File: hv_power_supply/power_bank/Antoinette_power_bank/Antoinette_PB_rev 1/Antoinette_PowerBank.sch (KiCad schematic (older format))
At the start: 44 parts, among them J1 NanoFit_RA_TH_02, J2 USB-Micro-1981568-1, J3 NanoFit_RA_TH_02, J4 USB-A-S-X-X-SM2, J5 NanoFit_RA_TH_02, Q1 SSM3K333R, U2 MCP73871T-2CCI_ML, U3 TPS61090RSAR

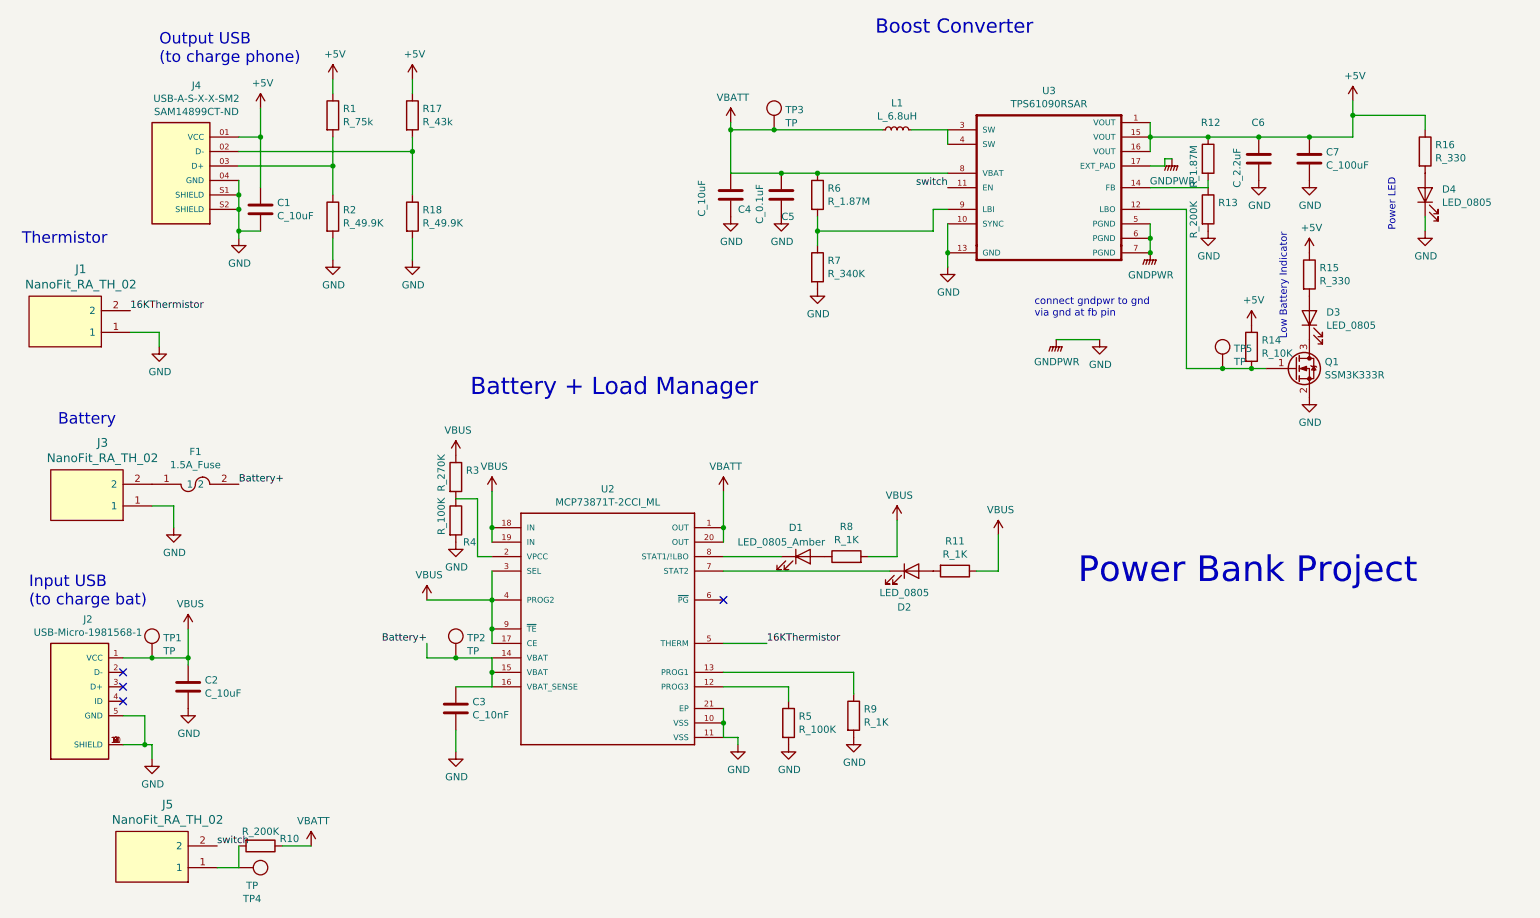
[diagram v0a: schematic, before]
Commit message: Add new files for updated pcb.
Added files for updated pcb with new inductor and series/parallel resistors for the 10k thermistor.
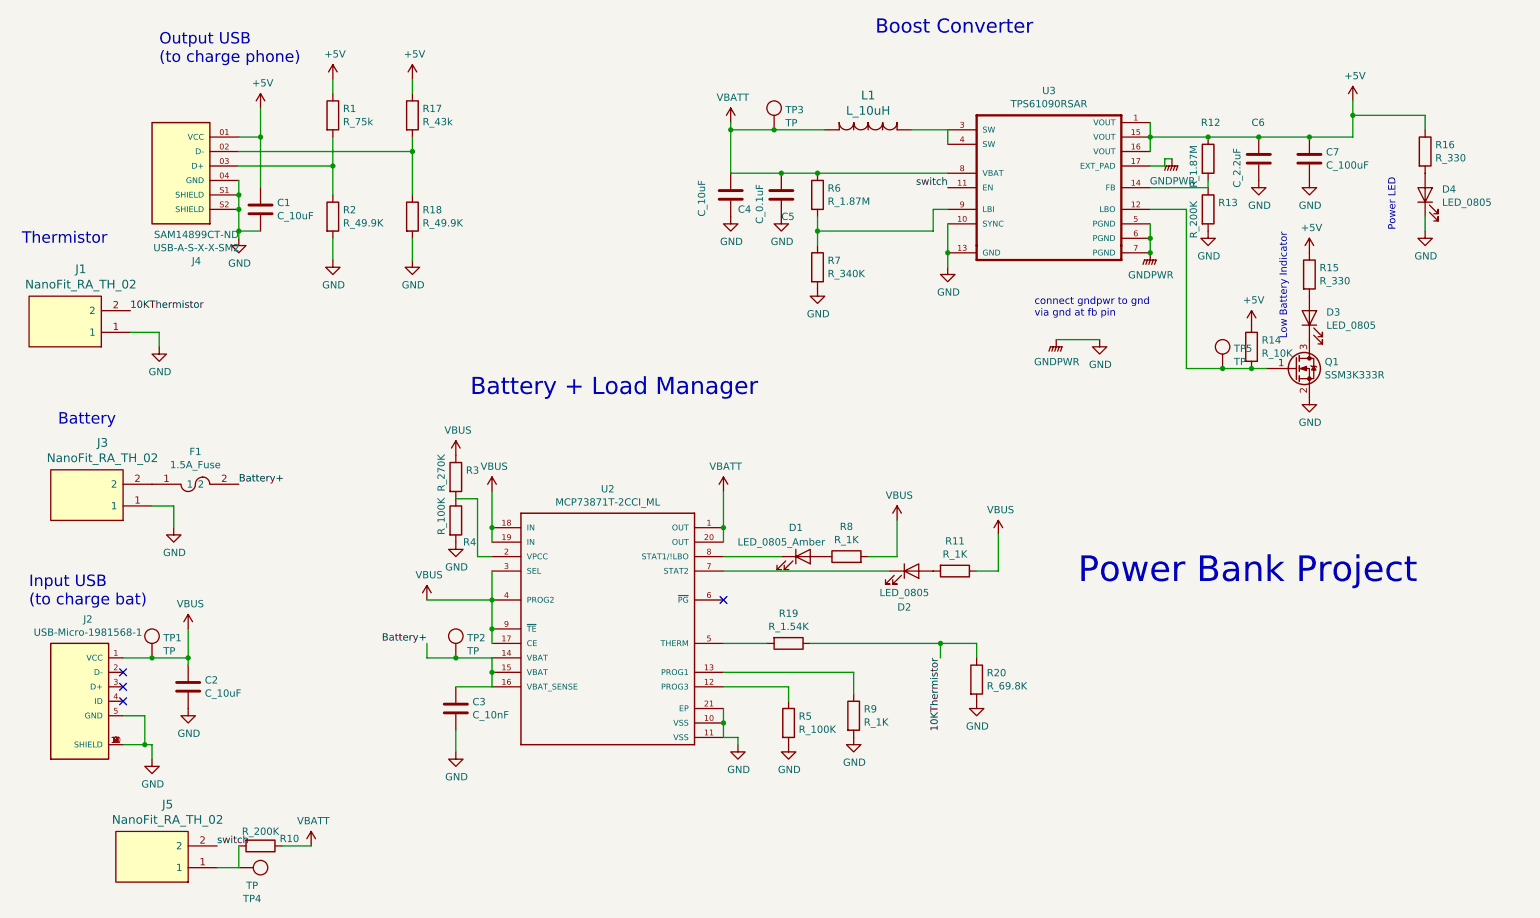
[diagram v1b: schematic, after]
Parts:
- removed L1: L_6.8uH, footprints:L_100uH_OEM, symbol formula:L_6.8uH
- added L1: L_10uH, footprints:BournsInductor, symbol formula:L_10uH
- added R19: R_1.54K, footprints:R_0805_OEM, symbol formula:R_1.54K
- added R20: R_69.8K, footprints:R_0805_OEM, symbol formula:R_69.8K
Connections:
- net +BATT: now also L1.2
- net GND: now also R20.2
- net at U3.3 (SW), U3.4 (SW): now also L1.1
- net 16KThermistor: no longer names the net of U2.5 (THERM)
- net 16KThermistor: now also R19.2; no longer J1.2
- new net 10KThermistor: J1.2, R19.1, R20.1
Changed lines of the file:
@@
 	1750 2900 1750 3000
 Text Label 1550 2750 0    50   ~ 0
-16KThermistor
+10KThermistor
 Text Label 2300 3950 0    50   ~ 0
 Battery+
@@
 	1    0    0    -1
 $EndComp
-$Comp
-L formula:L_6.8uH L1
-U 1 1 5F93B925
-P 6850 1500
-F 0 "L1" H 6850 1685 50  0000 C CNN
-F 1 "L_6.8uH" H 6850 1594 50  0000 C CNN
-F 2 "footprints:L_100uH_OEM" H 6750 1300 50  0001 C CNN
-F 3 "" H 6750 1350 50  0001 C CNN
-F 4 "Digikey" H 6950 1300 50  0001 C CNN "MFN"
-F 5 "445-1539-1-ND" H 6850 1750 50  0001 C CNN "MPN"
-	1    6850 1500
-	1    0    0    -1
-$EndComp
 Wire Wire Line
 	7200 1500 6950 1500
@@
 Wire Wire Line
 	5650 5050 5950 5050
-Text Label 5950 5050 0    50   ~ 0
-16KThermistor
+Text Label 7150 5150 3    50   ~ 0
+10KThermistor
 NoConn ~ 5650 4750
 Wire Wire Line
@@
 Text Notes 8100 4650 0    177  ~ 0
 Power Bank Project
-$Comp
-L formula:USB-A-S-X-X-SM2 J4
-U 1 1 5FB17265
-P 1900 1750
-F 0 "J4" H 1793 2307 50  0000 C CNN
-F 1 "USB-A-S-X-X-SM2" H 1793 2216 50  0000 C CNN
-F 2 "footprints:SAMTEC_USB-A-S-X-X-SM2" H 1900 1750 50  0001 L BNN
-F 3 "http://suddendocs.samtec.com/catalog_english/usb_a.pdf" H 1900 1750 50  0001 L BNN
-F 4 "Samtec" H 1900 1750 50  0001 L BNN "Field4"
-F 5 "Manufacturer Recommendations" H 1900 1750 50  0001 L BNN "Field5"
-F 6 "7.8 mm" H 1900 1750 50  0001 L BNN "Field6"
-F 7 "SAM14899CT-ND" H 1793 2125 50  0000 C CNN "MPN"
-	1    1900 1750
-	-1   0    0    -1
-$EndComp
 Wire Wire Line
 	1500 5750 1650 5750
-$Comp
-L formula:USB-Micro-1981568-1 J2
-U 1 1 5FB0DC42
-P 1200 5450
-F 0 "J2" H 1257 6017 50  0000 C CNN
-F 1 "USB-Micro-1981568-1" H 1257 5926 50  0000 C CNN
-F 2 "footprints:TE_1981568-1" H 1000 6000 50  0001 L BNN
-F 3 "https://www.te.com/commerce/DocumentDelivery/DDEController?Action=srchrtrv&DocNm=1981568&DocType=Customer+Drawing&DocLang=English" H 1200 5450 50  0001 L BNN
-F 4 ".65 mm[.025 in]" H 1150 6000 50  0001 L BNN "Field4"
-F 5 "Connector" H 600 5800 50  0001 L BNN "Field5"
-F 6 "1981568-1" H 1100 6000 50  0001 L BNN "Field6"
-F 7 "1981568-1" H 1350 5900 50  0001 C CNN "MPN"
-F 8 "https://www.digikey.com/en/products/detail/te-connectivity-amp-connectors/1981568-1/1786248?s=N4IgTCBcDaIIwE4AccCsA2JBaOIC6AvkA" H 1000 6000 50  0001 C CNN "Purchasing Link"
-	1    1200 5450
-	1    0    0    -1
-$EndComp
 Wire Wire Line
 	1500 5550 1650 5550
@@
 	5650 4000 5650 4250
 Wire Wire Line
-	2300 1850 2300 1950
-Wire Wire Line
 	5700 1800 6050 1800
 Wire Wire Line
@@
 Wire Wire Line
 	6300 1800 7200 1800
-Connection ~ 6000 1500
-Wire Wire Line
-	6000 1500 6750 1500
 Connection ~ 9700 1550
 Wire Wire Line
@@
 Wire Wire Line
 	7200 2350 7200 2450
-Connection ~ 2300 2050
-Wire Wire Line
-	2300 2050 2300 2200
-Connection ~ 2300 1950
-Wire Wire Line
-	2300 1950 2300 2050
 Connection ~ 5650 5600
 Wire Wire Line
@@
 	-1   0    0    1
 $EndComp
+$Comp
+L formula:USB-A-S-X-X-SM2 J4
+U 1 1 606F9F4E
+P 1900 1750
+F 0 "J4" H 1793 1093 50  0000 C CNN
+F 1 "USB-A-S-X-X-SM2" H 1793 1184 50  0000 C CNN
+F 2 "footprints:SAMTEC_USB-A-S-X-X-SM2" H 1900 1750 50  0001 L BNN
+F 3 "" H 1900 1750 50  0001 L BNN
+F 4 "Samtec" H 1900 1750 50  0001 L BNN "Field4"
+F 5 "Manufacturer Recommendations" H 1900 1750 50  0001 L BNN "Field5"
+F 6 "7.8 mm" H 1900 1750 50  0001 L BNN "Field6"
+F 7 "SAM14899CT-ND" H 1793 1275 50  0000 C CNN "MPN"
+	1    1900 1750
+	-1   0    0    -1
+$EndComp
+Wire Wire Line
+	2300 1850 2300 1950
+Wire Wire Line
+	2300 2050 2300 2200
+$Comp
+L formula:USB-Micro-1981568-1 J2
+U 1 1 60708014
+P 1200 5450
+F 0 "J2" H 1257 6017 50  0000 C CNN
+F 1 "USB-Micro-1981568-1" H 1257 5926 50  0000 C CNN
+F 2 "footprints:TE_1981568-1" H 1000 6000 50  0001 L BNN
+F 3 "" H 1200 5450 50  0001 L BNN
+F 4 ".65 mm[.025 in]" H 1150 6000 50  0001 L BNN "Field4"
+F 5 "Connector" H 600 5800 50  0001 L BNN "Field5"
+F 6 "1981568-1" H 1100 6000 50  0001 L BNN "Field6"
+F 7 "1981568-1" H 1350 5900 50  0001 C CNN "MPN"
+F 8 "https://www.digikey.com/en/products/detail/te-connectivity-amp-connectors/1981568-1/1786248?s=N4IgTCBcDaIIwE4AccCsA2JBaOIC6AvkA" H 1000 6000 50  0001 C CNN "Purchasing Link"
+	1    1200 5450
+	1    0    0    -1
+$EndComp
+$Comp
+L formula:L_10uH L1
+U 1 1 6071EE73
+P 6350 1500
+F 0 "L1" H 6650 1738 60  0000 C CNN
+F 1 "L_10uH" H 6650 1632 60  0000 C CNN
+F 2 "footprints:BournsInductor" H 6625 1215 60  0001 C CNN
+F 3 "https://www.bourns.com/docs/Product-Datasheets/SDE0805A.pdf" H 6350 1500 60  0001 C CNN
+F 4 "https://www.digikey.com/en/products/detail/bourns-inc/SDE0805A-100M/5030885" H 6350 1500 50  0001 C CNN "Purchasing"
+F 5 "SDE0805A-100M" H 6350 1500 50  0001 C CNN "MPN"
+F 6 "Bourns Inc." H 6350 1500 50  0001 C CNN "MFN"
+	1    6350 1500
+	1    0    0    -1
+$EndComp
+Wire Wire Line
+	6350 1500 6000 1500
+Connection ~ 6000 1500
+$Comp
+L formula:R_1.54K R19
+U 1 1 6072D45A
+P 6100 5050
+F 0 "R19" V 5893 5050 50  0000 C CNN
+F 1 "R_1.54K" V 5984 5050 50  0000 C CNN
+F 2 "footprints:R_0805_OEM" H 6030 5050 50  0001 C CNN
+F 3 "https://industrial.panasonic.com/cdbs/www-data/pdf/RDA0000/AOA0000C304.pdf" H 6180 5050 50  0001 C CNN
+F 4 "Panasonic" H 6100 5050 50  0001 C CNN "MFN"
+F 5 "ERJ-6ENF1541V" H 6100 5050 50  0001 C CNN "MPN"
+F 6 "https://www.digikey.com/en/products/detail/panasonic-electronic-components/ERJ-6ENF1541V/111317" H 6100 5050 50  0001 C CNN "Purchasing Link"
+	1    6100 5050
+	0    1    1    0
+$EndComp
+$Comp
+L formula:R_69.8K R20
+U 1 1 6072E92F
+P 7400 5300
+F 0 "R20" H 7470 5346 50  0000 L CNN
+F 1 "R_69.8K" H 7470 5255 50  0000 L CNN
+F 2 "footprints:R_0805_OEM" H 7330 5300 50  0001 C CNN
+F 3 "https://industrial.panasonic.com/cdbs/www-data/pdf/RDA0000/AOA0000C304.pdf" H 7480 5300 50  0001 C CNN
+F 4 "ERJ-6ENF6982V" H 7400 5300 50  0001 C CNN "MPN"
+F 5 "Panasonic Electronic Components" H 7400 5300 50  0001 C CNN "MFN"
+F 6 "https://www.digikey.com/en/products/detail/panasonic-electronic-components/ERJ-6ENF6982V/111648" H 7400 5300 50  0001 C CNN "Purchasing"
+	1    7400 5300
+	1    0    0    -1
+$EndComp
+Wire Wire Line
+	6250 5050 7150 5050
+Wire Wire Line
+	7400 5050 7400 5150
+Wire Wire Line
+	7150 5150 7150 5050
+Connection ~ 7150 5050
+Wire Wire Line
+	7150 5050 7400 5050
+$Comp
+L power:GND #PWR0117
+U 1 1 607413C5
+P 7400 5450
+F 0 "#PWR0117" H 7400 5200 50  0001 C CNN
+F 1 "GND" H 7405 5277 50  0000 C CNN
+F 2 "" H 7400 5450 50  0001 C CNN
+F 3 "" H 7400 5450 50  0001 C CNN
+	1    7400 5450
+	1    0    0    -1
+$EndComp
+Wire Wire Line
+	2300 2050 2300 1950
+Connection ~ 2300 2050
+Connection ~ 2300 1950
 $EndSCHEMATC
